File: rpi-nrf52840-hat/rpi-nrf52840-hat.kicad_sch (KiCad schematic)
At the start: 27 parts, among them J1 Conn_02x04_Odd_Even, J2 Raspberry_Pi_4, J3 Conn_02x04_Odd_Even, U1 E73-2G4M08S1C, U2 24C32, X1 32.768kHz 12.5pF

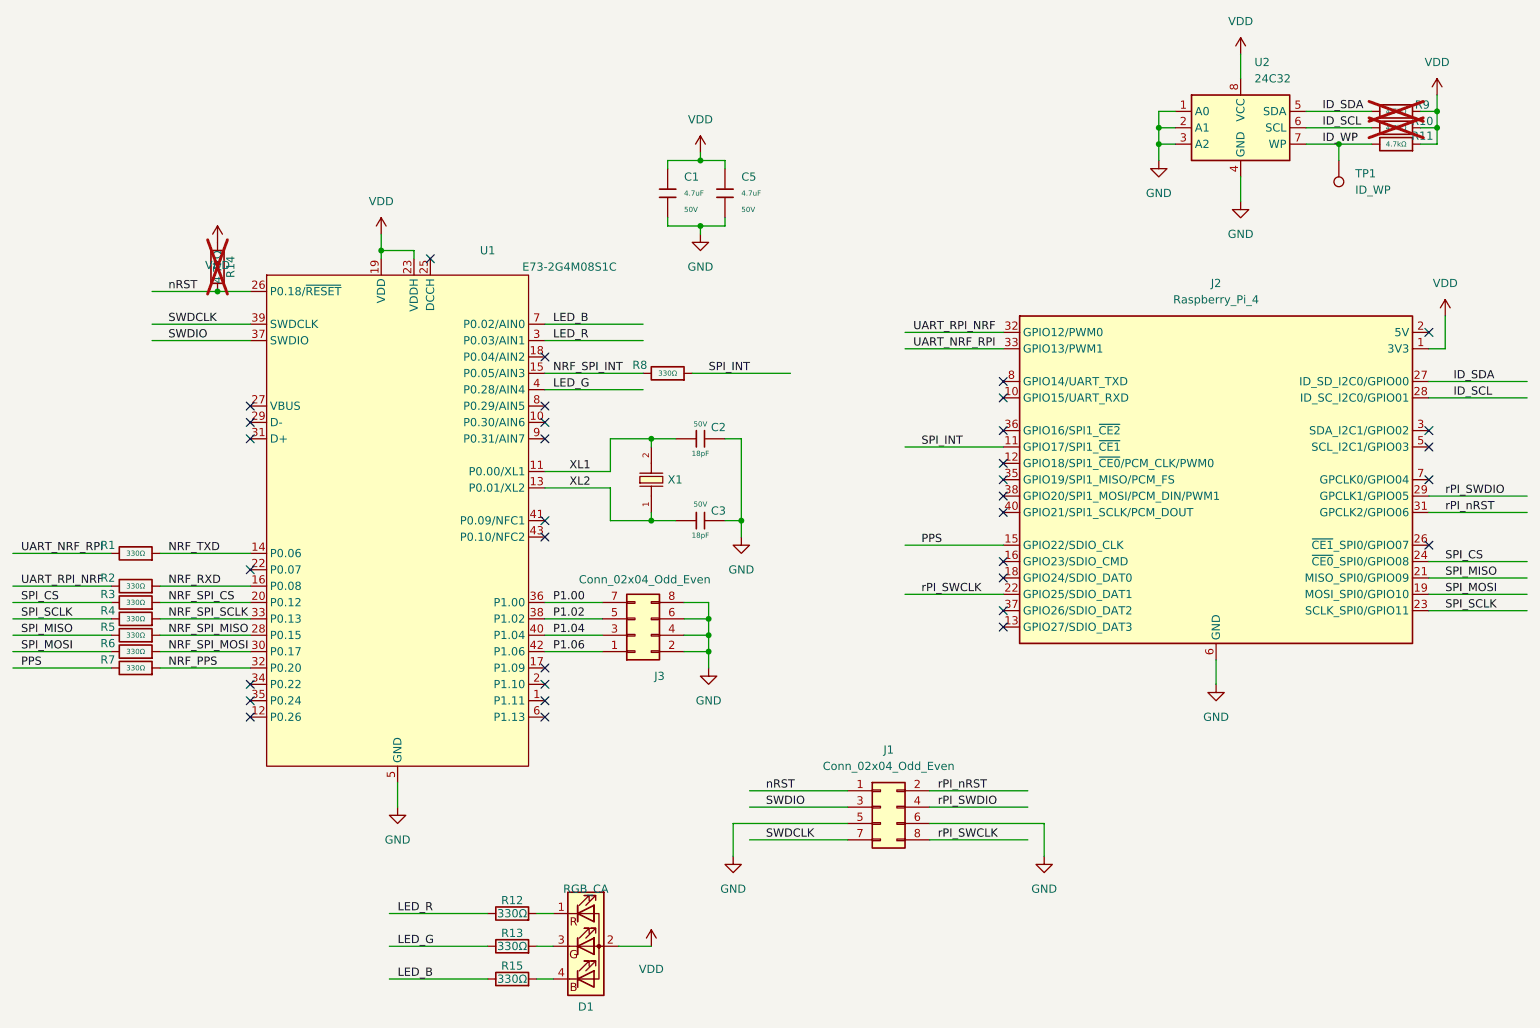
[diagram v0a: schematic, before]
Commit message: remove populate_jlc_library and convert to kifab
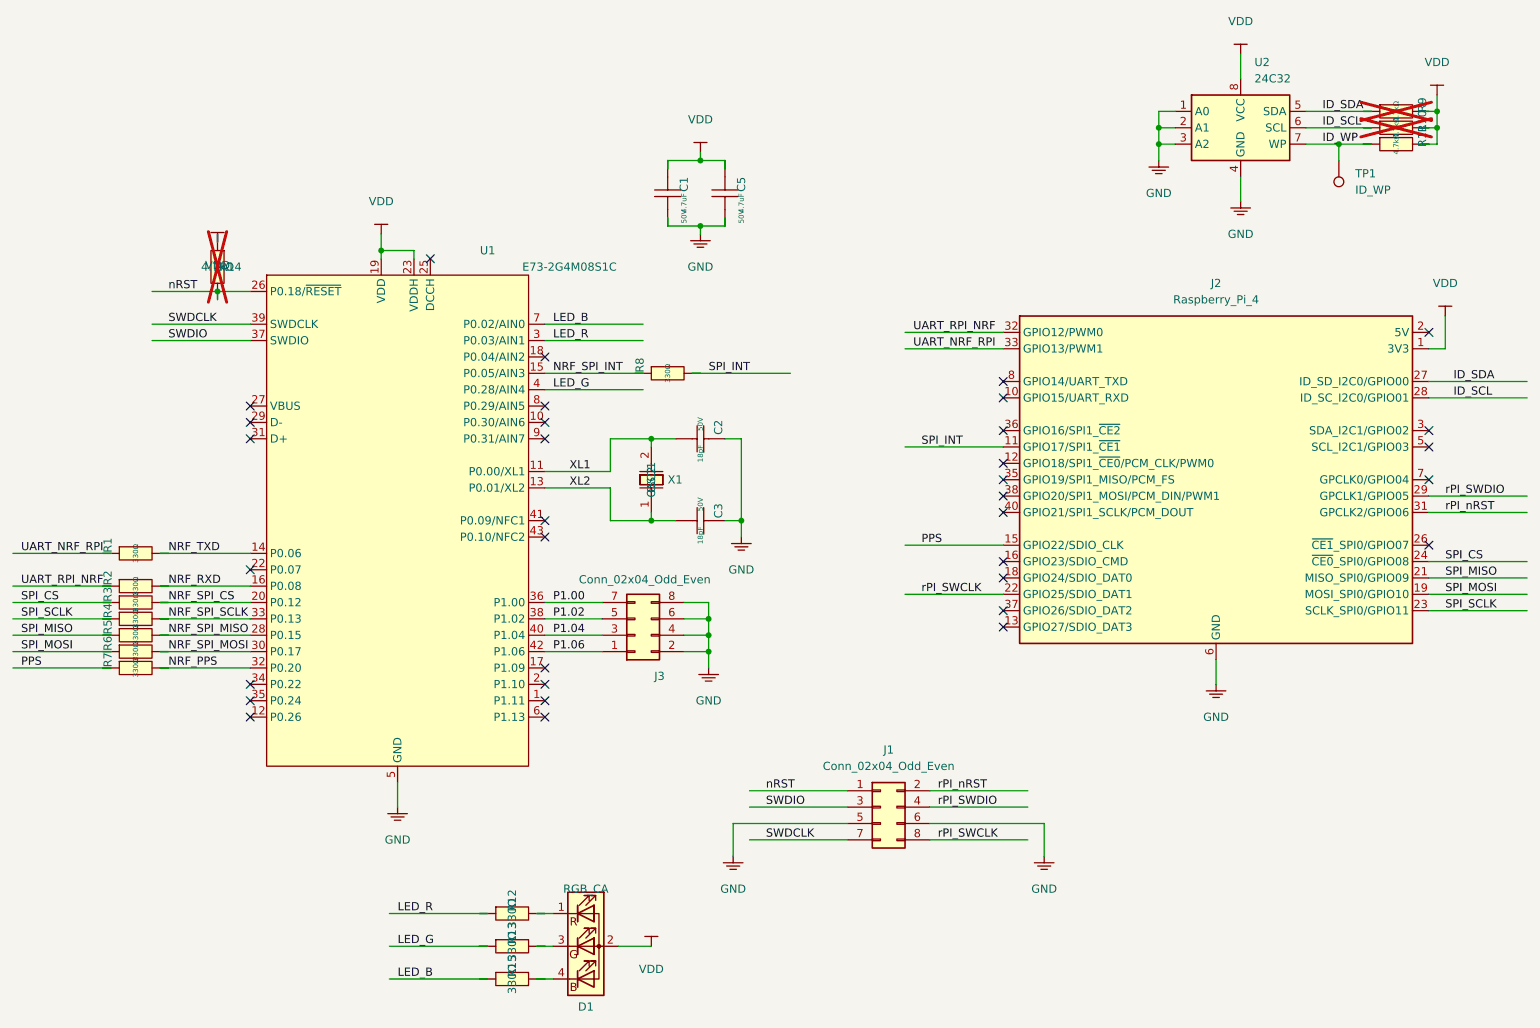
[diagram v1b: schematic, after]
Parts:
- C1, C5: symbol PCM_JLCPCB-Capacitors:1206,4.7uF -> jlcpcb:TCC0805X7R475K500FT
- C2, C3: symbol PCM_JLCPCB-Capacitors:0603,12pF -> jlcpcb:CL10C180JB8NNNC
- D1: footprint rpi-nrf52840-hat:LED_RGB_1.6x1.5mm_CA_P4-1615 -> project:LED_RGB_1.6x1.5mm_CA_P4-1615; symbol Device:LED_RAGB -> project:LED_RAGB
- J1, J3: footprint Connector_PinHeader_2.54mm:PinHeader_2x04_P2.54mm_Vertical -> project:PinHeader_2x04_P2.54mm_Vertical; symbol Connector_Generic:Conn_02x04_Odd_Even -> project:Conn_02x04_Odd_Even
- J2: footprint Connector_PinSocket_2.54mm:PinSocket_2x20_P2.54mm_Vertical -> project:PinSocket_2x20_P2.54mm_Vertical; symbol Connector:Raspberry_Pi_4 -> project:Raspberry_Pi_4
- R1, R12, R13, R15, R2, R3, R4, R5, R6, R7, R8: symbol Device:R -> jlcpcb:0603WAF3300T5E
- R10, R11, R14, R9: symbol Device:R -> jlcpcb:0603WAF4701T5E
- TP1: footprint Connector_PinHeader_2.54mm:PinHeader_1x01_P2.54mm_Vertical -> project:PinHeader_1x01_P2.54mm_Vertical; symbol Connector:TestPoint -> project:TestPoint
- U1: symbol PCM_nordic-lib-kicad-nrf52-modules:E73-2G4M08S1C -> project:E73-2G4M08S1C
- U2: symbol Memory_EEPROM:24C02Cx-x-SN -> project:24C02Cx-x-SN
- X1: symbol PCM_JLCPCB-Crystals:Crystal, 32.768kHz, 13pF -> jlcpcb:CC7V-T1A-32.768KHZ-12.5PF-20PPM-TA-QC
